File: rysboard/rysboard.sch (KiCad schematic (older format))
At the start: 13 parts, among them J1 RPi4, J17 Conn_01x03, Q1 BC847BS

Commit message: rysboard: add PWM fan output
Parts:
- added D10: 1N4148, Diode_SMD:D_0603_1608Metric, symbol Diode:1N4148
- added J18: Conn_01x02, Connector_PinHeader_2.54mm:PinHeader_1x02_P2.54mm_Vertical, symbol Connector_Generic:Conn_01x02
- added Q2: BC817, Package_TO_SOT_SMD:SOT-23, symbol Transistor_BJT:BC817
- added R15: 680R, Resistor_SMD:R_0603_1608Metric, symbol Device:R
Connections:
- net labels added: FAN_PWM
- wire segments 85 -> 97
- no-connect marks 3 -> 2
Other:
- note added: "Cooling Fan"
- moved on the sheet: D6, D7, J17, R10, R11, R12, R7

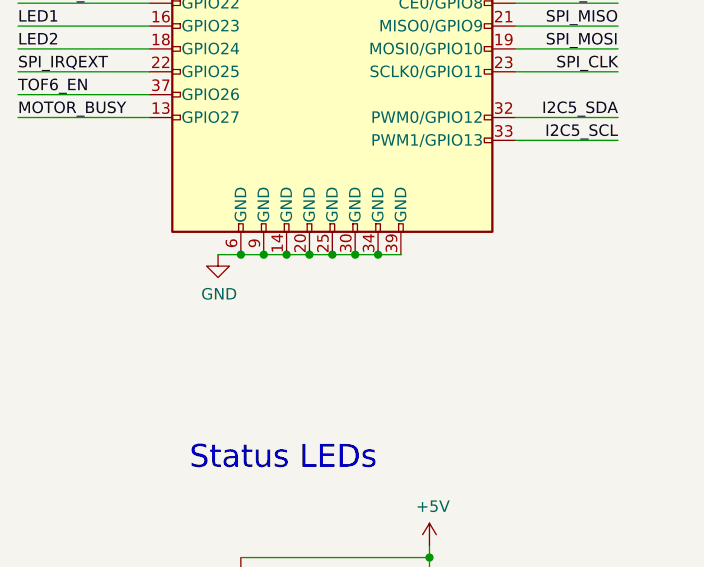
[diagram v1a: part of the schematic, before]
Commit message: rysboard: move D8 before converter feedback; replace U5 with counterpart of higher availability; fix U4 wiring; improve GND connections to motor drivers
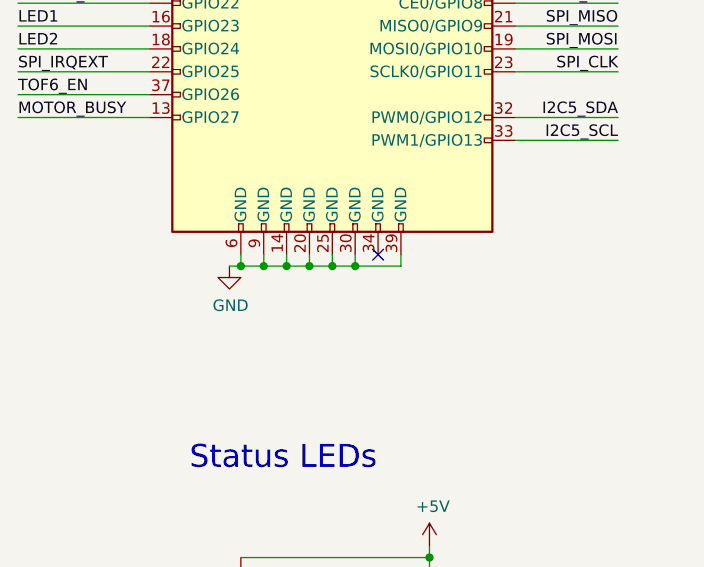
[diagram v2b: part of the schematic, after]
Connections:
- wire segments 97 -> 103
- no-connect marks 2 -> 3
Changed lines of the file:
@@
 	1    0    0    -1
 $EndComp
-Wire Wire Line
-	2975 1650 2875 1650
 $Comp
 L power:+3V3 #PWR03
@@
 	1    0    0    -1
 $EndComp
-Wire Wire Line
-	3175 1650 3275 1650
-$Comp
-L power:GND #PWR01
-U 1 1 5EB9309D
-P 2575 4250
-F 0 "#PWR01" H 2575 4000 50  0001 C CNN
-F 1 "GND" H 2580 4077 50  0000 C CNN
-F 2 "" H 2575 4250 50  0001 C CNN
-F 3 "" H 2575 4250 50  0001 C CNN
-	1    2575 4250
-	1    0    0    -1
-$EndComp
-Wire Wire Line
-	2875 4250 2975 4250
-Connection ~ 2875 4250
-Connection ~ 2975 4250
-Wire Wire Line
-	3175 4250 3275 4250
-Connection ~ 3175 4250
-Wire Wire Line
-	3275 4250 3375 4250
-Connection ~ 3275 4250
 Wire Wire Line
 	3875 3150 4325 3150
@@
 Wire Wire Line
 	1700 3450 2275 3450
-Connection ~ 2875 1650
-Connection ~ 3275 1650
-Wire Wire Line
-	2575 4250 2675 4250
-Connection ~ 2675 4250
-Wire Wire Line
-	2675 4250 2775 4250
-Wire Wire Line
-	2875 4250 2775 4250
-Connection ~ 2775 4250
-Wire Wire Line
-	2975 4250 3075 4250
-Wire Wire Line
-	3075 4250 3175 4250
-Connection ~ 3075 4250
-Wire Wire Line
-	3275 1650 3525 1650
-Wire Wire Line
-	2625 1650 2875 1650
-$Comp
-L Connector:Raspberry_Pi_2_3 J1
-U 1 1 5EA5D2E2
-P 3075 2950
-F 0 "J1" H 3075 4431 50  0000 C CNN
-F 1 "RPi4" H 3075 4340 50  0000 C CNN
-F 2 "Connector_PinSocket_2.54mm:PinSocket_2x20_P2.54mm_Vertical" H 3075 2950 50  0001 C CNN
-F 3 "https://www.raspberrypi.org/documentation/hardware/raspberrypi/schematics/rpi_SCH_3bplus_1p0_reduced.pdf" H 3075 2950 50  0001 C CNN
-	1    3075 2950
-	1    0    0    -1
-$EndComp
 $Sheet
 S 8250 1500 975  600
@@
 	0    1    1    0
 $EndComp
+Wire Wire Line
+	3175 1650 3275 1650
+Wire Wire Line
+	2975 1650 2875 1650
+$Comp
+L power:GND #PWR01
+U 1 1 5EB9309D
+P 2625 4300
+F 0 "#PWR01" H 2625 4050 50  0001 C CNN
+F 1 "GND" H 2630 4127 50  0000 C CNN
+F 2 "" H 2625 4300 50  0001 C CNN
+F 3 "" H 2625 4300 50  0001 C CNN
+	1    2625 4300
+	1    0    0    -1
+$EndComp
+Wire Wire Line
+	2625 4300 2675 4300
+Wire Wire Line
+	2675 4300 2675 4250
+Connection ~ 2875 1650
+Connection ~ 3275 1650
+Wire Wire Line
+	3275 1650 3525 1650
+Wire Wire Line
+	2625 1650 2875 1650
+$Comp
+L Connector:Raspberry_Pi_2_3 J1
+U 1 1 5EA5D2E2
+P 3075 2950
+F 0 "J1" H 3075 4431 50  0000 C CNN
+F 1 "RPi4" H 3075 4340 50  0000 C CNN
+F 2 "Connector_PinSocket_2.54mm:PinSocket_2x20_P2.54mm_Vertical" H 3075 2950 50  0001 C CNN
+F 3 "https://www.raspberrypi.org/documentation/hardware/raspberrypi/schematics/rpi_SCH_3bplus_1p0_reduced.pdf" H 3075 2950 50  0001 C CNN
+	1    3075 2950
+	1    0    0    -1
+$EndComp
+NoConn ~ 3275 4250
+Wire Wire Line
+	3375 4250 3375 4300
+Wire Wire Line
+	3375 4300 3175 4300
+Connection ~ 2675 4300
+Wire Wire Line
+	2775 4250 2775 4300
+Connection ~ 2775 4300
+Wire Wire Line
+	2775 4300 2675 4300
+Wire Wire Line
+	2875 4250 2875 4300
+Connection ~ 2875 4300
+Wire Wire Line
+	2875 4300 2775 4300
+Wire Wire Line
+	2975 4250 2975 4300
+Connection ~ 2975 4300
+Wire Wire Line
+	2975 4300 2875 4300
+Wire Wire Line
+	3075 4250 3075 4300
+Connection ~ 3075 4300
+Wire Wire Line
+	3075 4300 2975 4300
+Wire Wire Line
+	3175 4250 3175 4300
+Connection ~ 3175 4300
+Wire Wire Line
+	3175 4300 3075 4300
 $EndSCHEMATC

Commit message: added Battery Baalancing, Reverse polarity protection circuits and skeleton of power managment
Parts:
- removed D10: 1N4148, Diode_SMD:D_0603_1608Metric, symbol Diode:1N4148
- removed D6: GREEN, LED_SMD:LED_0805_2012Metric, symbol Device:LED
- removed D7: RED, LED_SMD:LED_0805_2012Metric, symbol Device:LED
- removed J18: Conn_01x02, Connector_PinHeader_2.54mm:PinHeader_1x02_P2.54mm_Vertical, symbol Connector_Generic:Conn_01x02
- removed Q1: BC847BS, Package_TO_SOT_SMD:SOT-363_SC-70-6, symbol Transistor_BJT:BC847BS
- removed Q2: BC817, Package_TO_SOT_SMD:SOT-23, symbol Transistor_BJT:BC817
- removed R10, R7: 10k, Resistor_SMD:R_0603_1608Metric, symbol Device:R
- removed R11, R12, R15: 680R, Resistor_SMD:R_0603_1608Metric, symbol Device:R
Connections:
- net labels added: RPI_5V
- net labels removed: +5V, LED1, LED2
- wire segments 103 -> 76
- no-connect marks 3 -> 5
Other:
- note removed: "Cooling Fan"
- note removed: "Status LEDs"
- moved on the sheet: J1

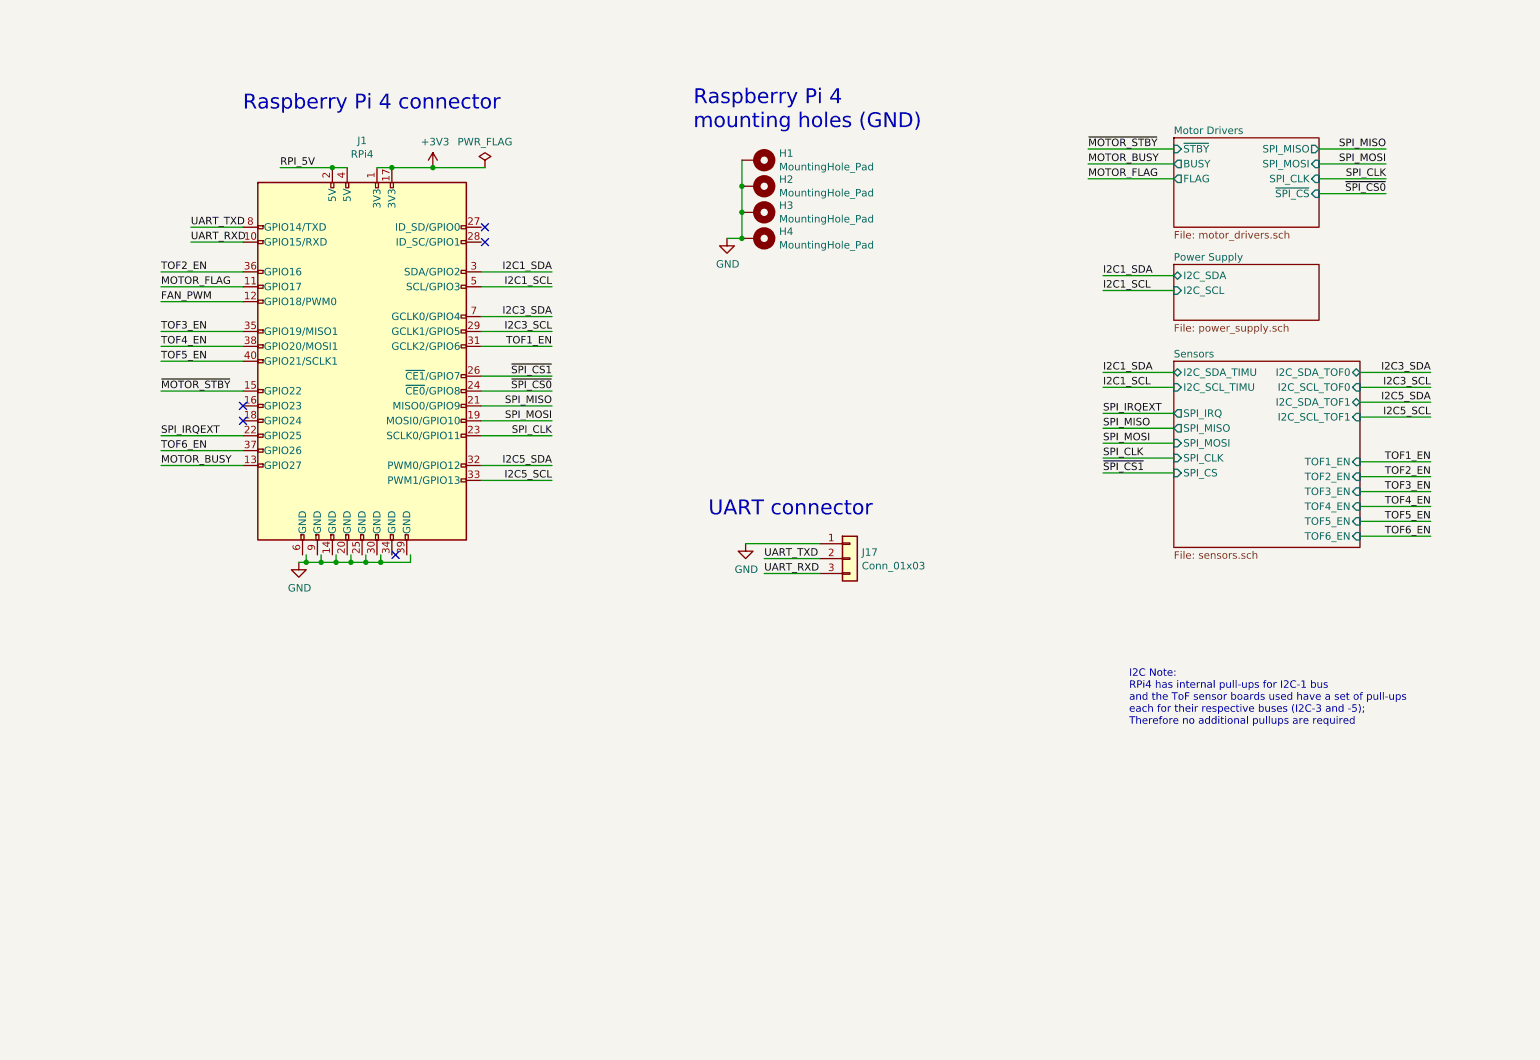
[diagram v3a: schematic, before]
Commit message: Added mcu, labeled its pins , major powwer supply overhaul started
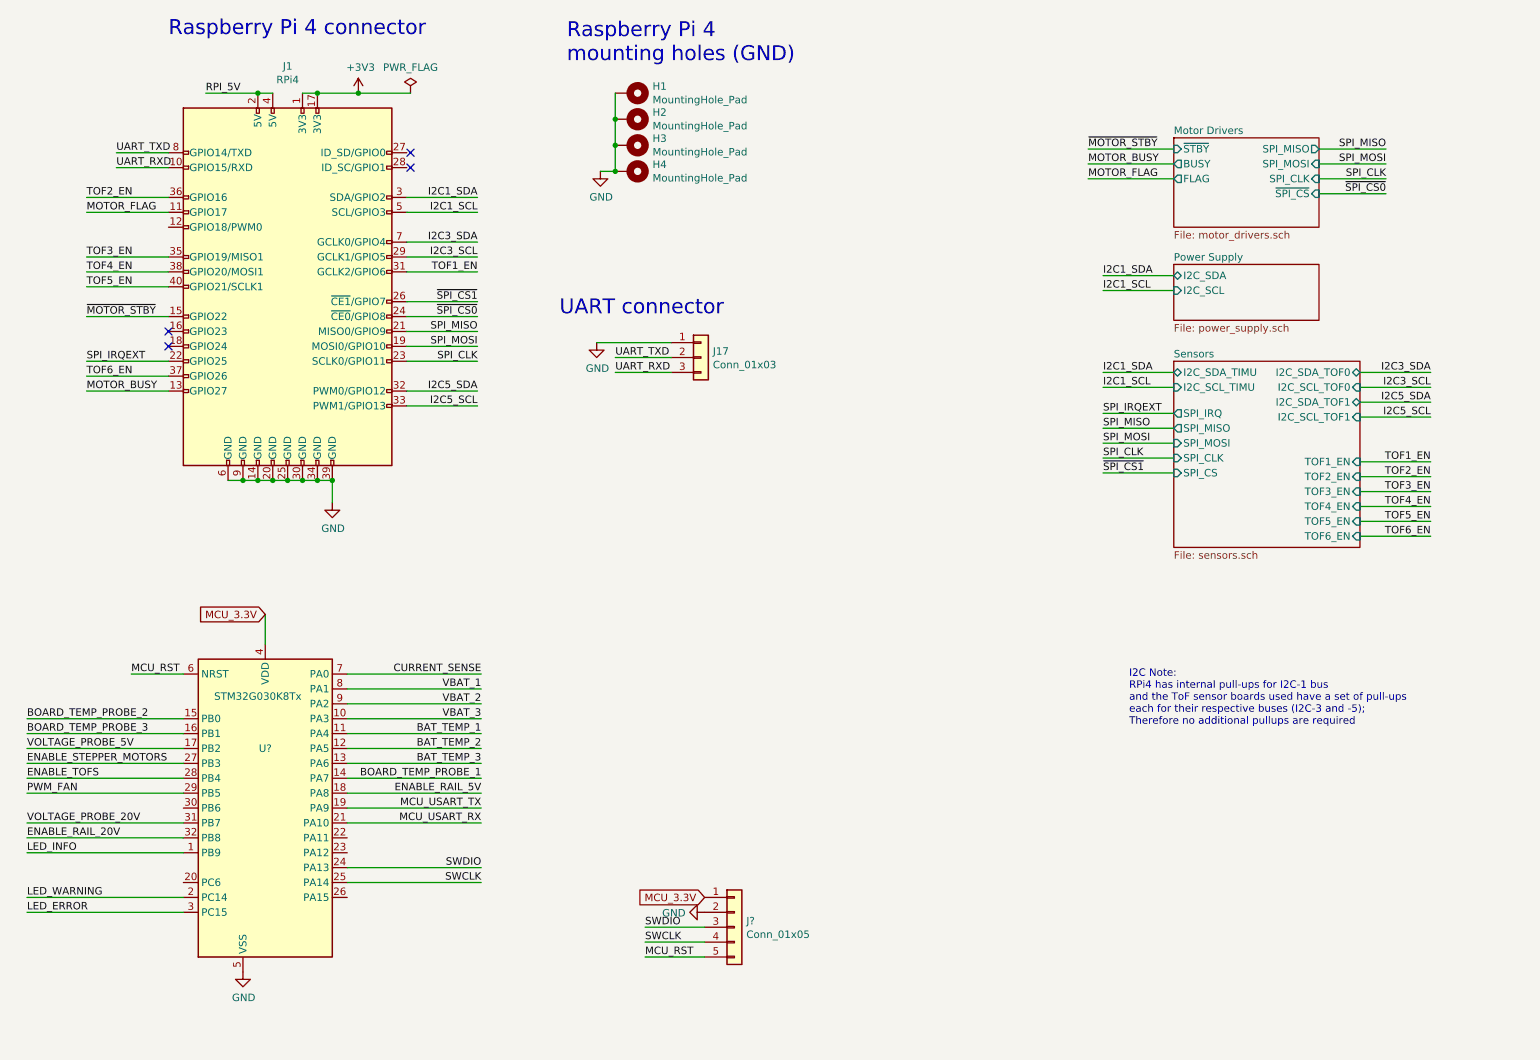
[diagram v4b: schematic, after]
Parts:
- added J?: Conn_01x05, Connector_PinHeader_1.00mm:PinHeader_1x05_P1.00mm_Vertical, symbol Connector_Generic:Conn_01x05
- added U?: STM32G030K8Tx, Package_QFP:LQFP-32_7x7mm_P0.8mm, symbol rysboard:STM32G030K8Tx
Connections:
- net labels added: BAT_TEMP_1, BAT_TEMP_2, BAT_TEMP_3, BOARD_TEMP_PROBE_1, BOARD_TEMP_PROBE_2, BOARD_TEMP_PROBE_3, CURRENT_SENSE, ENABLE_RAIL_20V, ENABLE_RAIL_5V, ENABLE_STEPPER_MOTORS, ENABLE_TOFS, LED_ERROR, LED_INFO, LED_WARNING, MCU_3.3V, MCU_RST, MCU_USART_RX, MCU_USART_TX, PWM_FAN, SWCLK, SWDIO, VBAT_1, VBAT_2, VBAT_3, VOLTAGE_PROBE_20V, VOLTAGE_PROBE_5V
- net labels removed: FAN_PWM
- wire segments 76 -> 98
- no-connect marks 5 -> 4
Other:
- moved on the sheet: H1, H2, H3, H4, J1, J17
